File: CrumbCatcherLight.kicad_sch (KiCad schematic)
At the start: 15 parts, among them J1 USB_C_Receptacle, J2 Mating Half to 51021-0300, J4 Qi Charger In, U0 PCB, U1 ECMF02-2AMX6

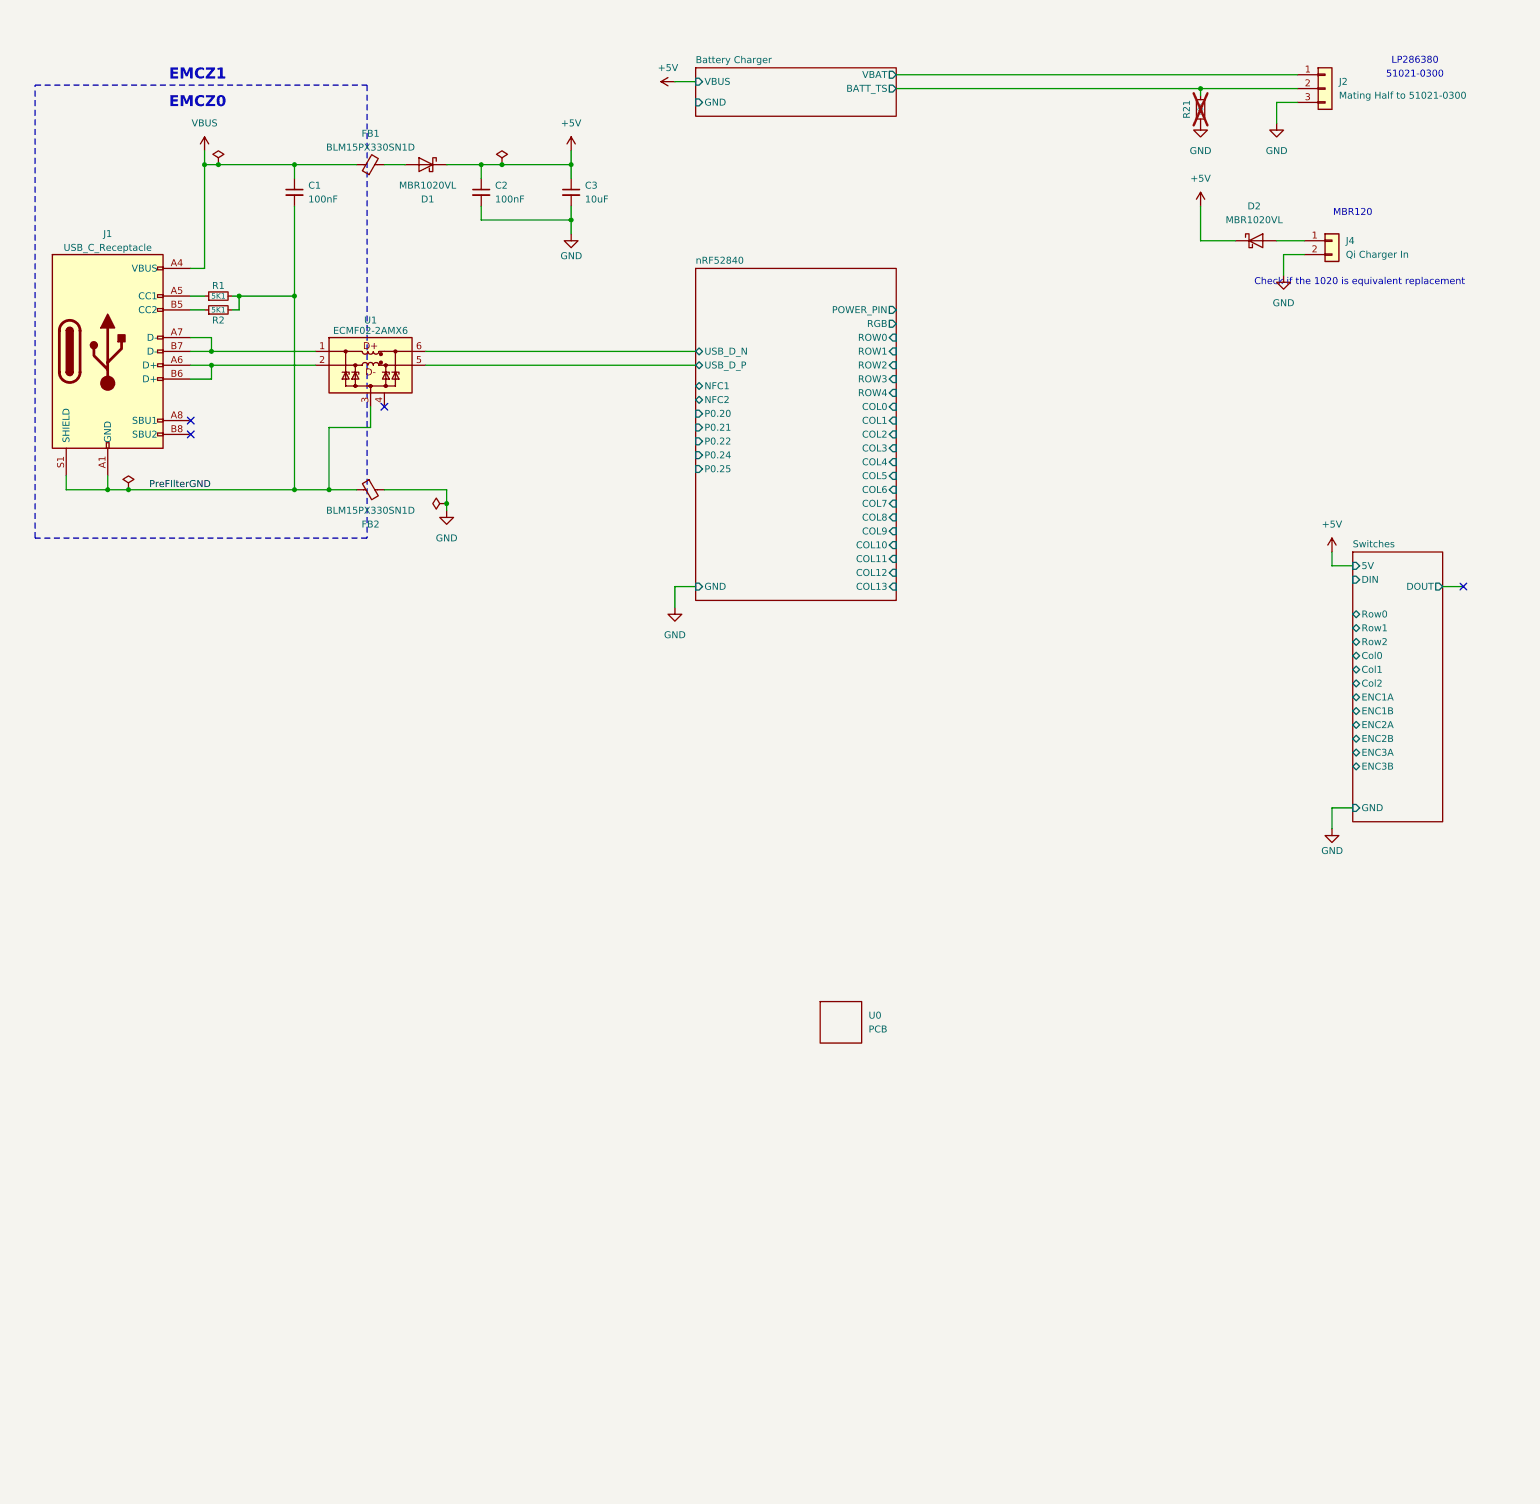
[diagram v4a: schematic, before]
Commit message: Add some todo notes, add 3/2 pin battery connectors
Add NTC connector, Update power scheme for RF module
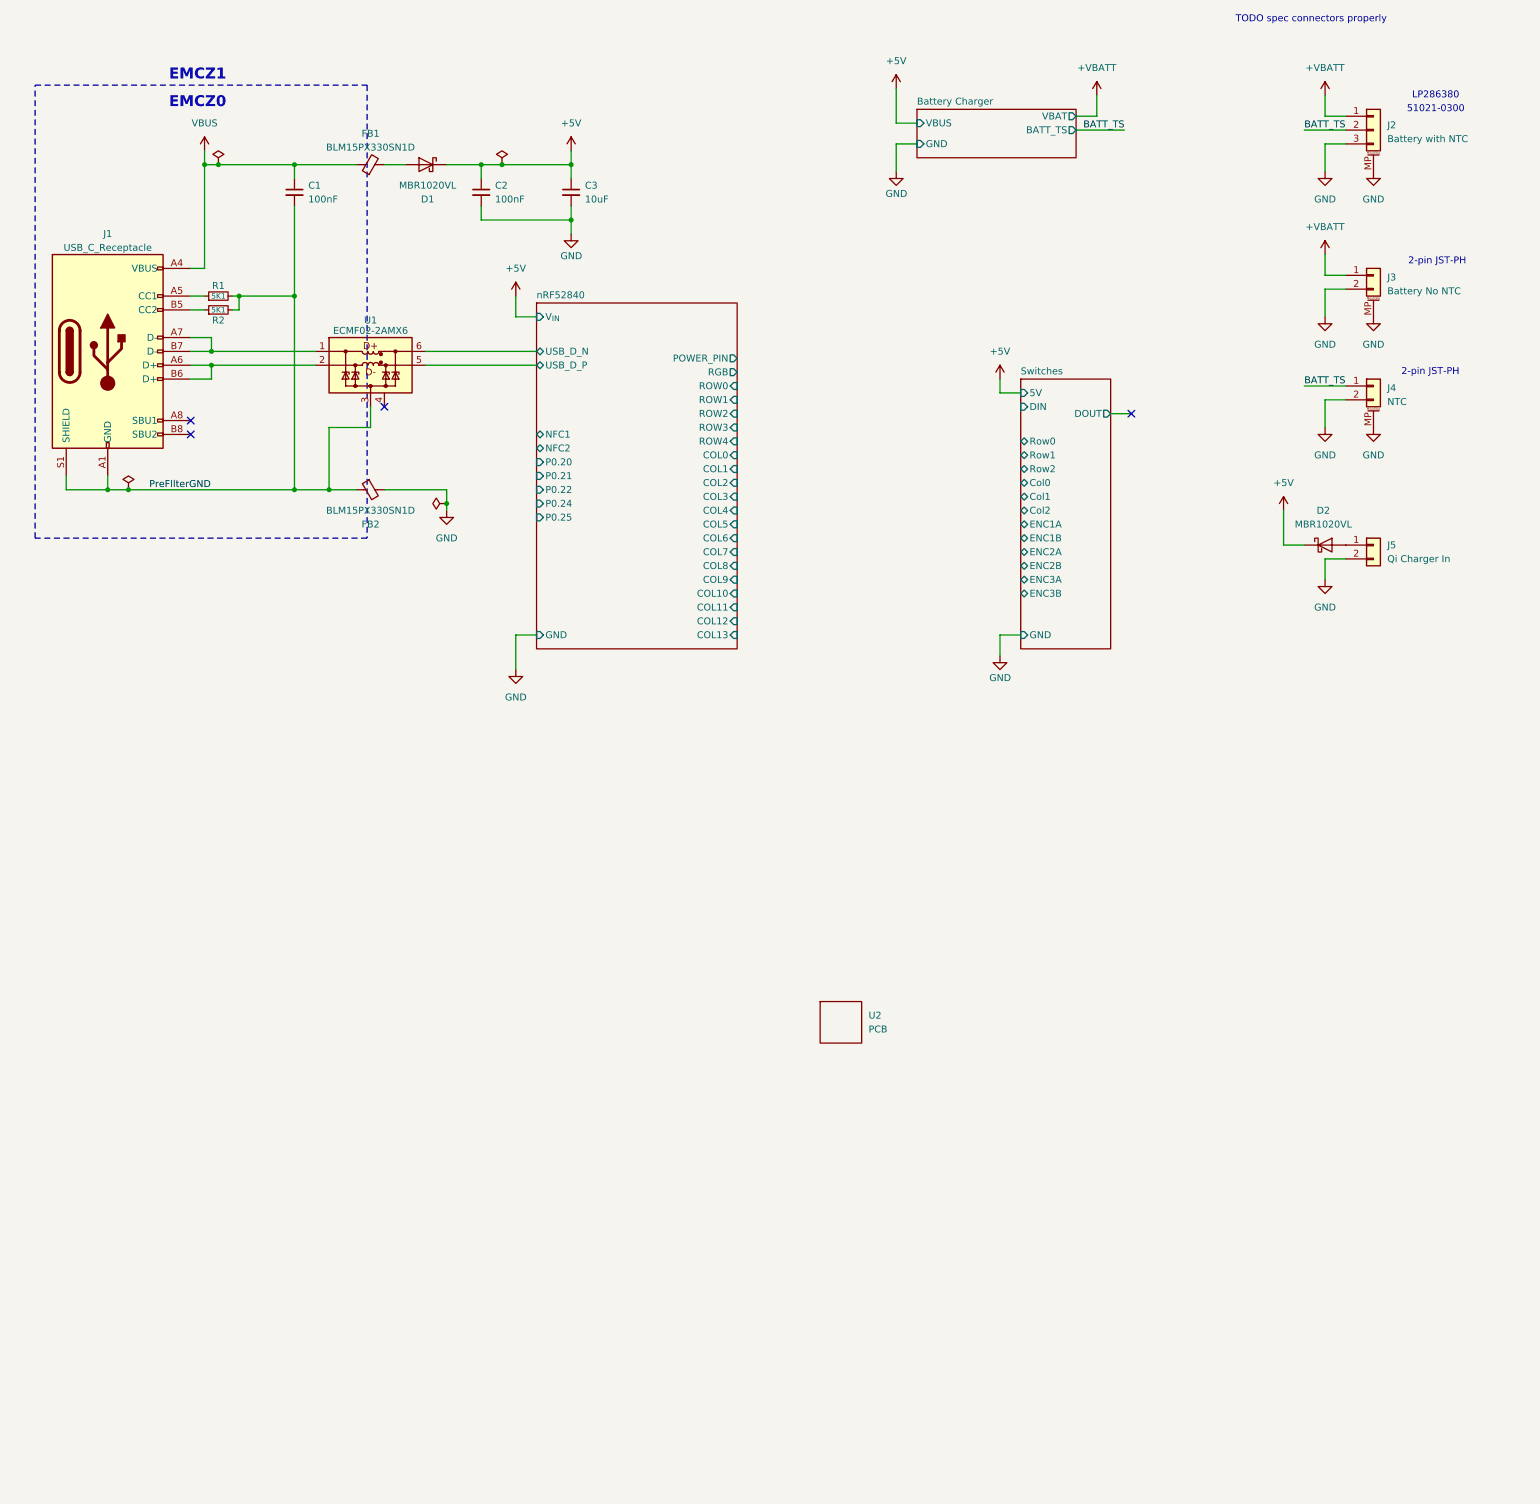
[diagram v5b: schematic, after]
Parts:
- removed R21: 10K, Resistor_SMD:R_0603_1608Metric, symbol Device:R_Small
- added J3: Battery No NTC, Connector_JST:JST_PH_B2B-PH-SM4-TB_1x02-1MP_P2.00mm_Vertical, symbol Connector_Generic_MountingPin:Conn_01x02_MountingPin
- added J4: NTC, Connector_JST:JST_PH_B2B-PH-SM4-TB_1x02-1MP_P2.00mm_Vertical, symbol Connector_Generic_MountingPin:Conn_01x02_MountingPin
- J2: value Mating Half to 51021-0300 -> Battery with NTC; symbol Connector_Generic:Conn_01x03 -> Connector_Generic_MountingPin:Conn_01x03_MountingPin
- renumbered J4 to J5, U0 to U2
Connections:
- net GND: now also J2.MP (MountPin), J3.2 (Pin_2), J3.MP (MountPin), J4.2 (Pin_2), J4.MP (MountPin)
- net Battery Charger/BATT_TS renamed BATT_TS
- net BATT_TS: now also J4.1 (Pin_1)
- net Battery Charger/VBAT renamed +VBATT
- net +VBATT: now also J3.1 (Pin_1)
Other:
- sheet nRF52840 ports: added V_{IN}; removed none
- note added: "2-pin JST-PH"
- note added: "TODO spec connectors properly"
- note removed: "Check if the 1020 is equivalent replacement"
- note removed: "MBR120"
- moved on the sheet: D2, J5

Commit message: Update BOM
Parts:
- C1, C2: footprint Capacitor_SMD:C_0402_1005Metric -> Capacitor_SMD:C_0603_1608Metric; LCSC (none) -> C432917; MPN CC0402KPX7R9BB104 -> CC0603KPX7R9BB104; Price $0.17 -> $0.10; Rating CAP 0402 50V 100 NF X7R -> CAP CER 0.1UF 50V X7R 0603; Supplier PN 13-CC0402KPX7R9BB104CT-ND -> (none); digikey (none) -> 311-3567-1-ND; mouser (none) -> 603-CC603KPX7R9BB104
- D1, D2: value MBR1020VL -> MBR120VL; MPN (none) -> MBR120VLSFT1G; Manufacturer (none) -> onsemi; Price (none) -> $0.41; Rating (none) -> DIODE SCHOTTKY 20V 1A SOD123FL; Supplier (none) -> Digikey; digikey (none) -> MBR120VLSFT1GOSCT-ND
- J2: now not fitted
- renumbered U2 to U0
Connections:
- net +5V: now also D2.2 (A), J5.1 (Pin_1)
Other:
- sheet Battery Charger ports: added BVOLT, VDDH, V_{BUS}; removed VBUS
- sheet nRF52840 ports: added VDDH, V_{BUS}; removed V_{IN}
- note removed: "EMCZ0"
- note removed: "EMCZ1"
- moved on the sheet: C3, D2, FB1, FB2, J1, J3, J4, J5, R1, R2, U0, U1

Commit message: Add some research, update switches
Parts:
- renumbered D2 to D1, D1 to D2, J5 to J2, J2 to J3, J3 to J4, J4 to J5, U0 to U2
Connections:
- no-connect marks 4 -> 3
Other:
- removed sheet Switches
- added sheet Untitled Sheet (untitled.kicad_sch)
